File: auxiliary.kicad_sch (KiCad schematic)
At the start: 70 parts, among them IC1 MAX1708EEE+, J4 BM04B-SRSS-TB-LF-SN, J5 SM06B-SRSS-TB(LF)(SN), J6 SM09B-SRSS-TB(LF)(SN), J7 61300611121, Q1 BSS138AKA, U1 PCA9547BS,118, U2 NTS0102DP

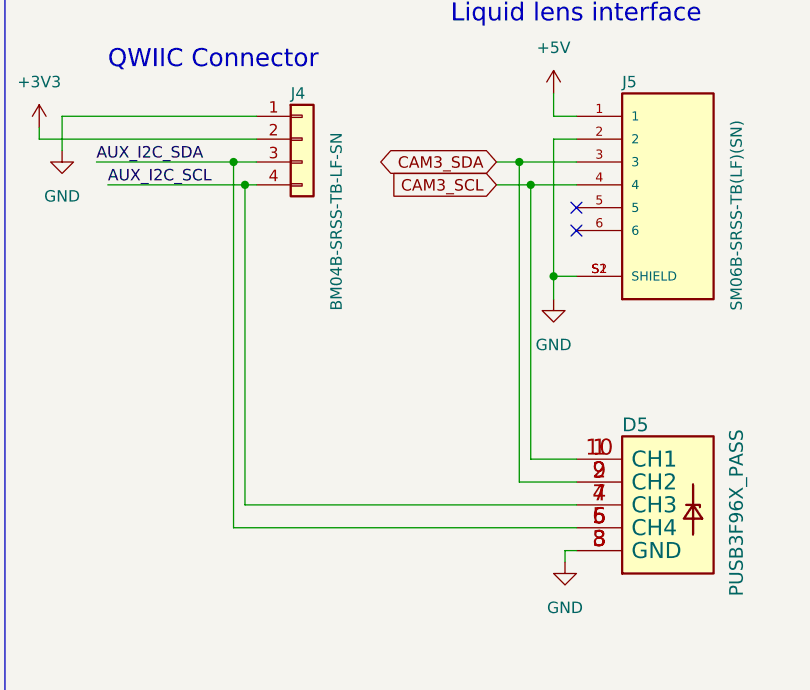
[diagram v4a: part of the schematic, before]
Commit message: Finished layout of most of the other signals, rerouted CSI
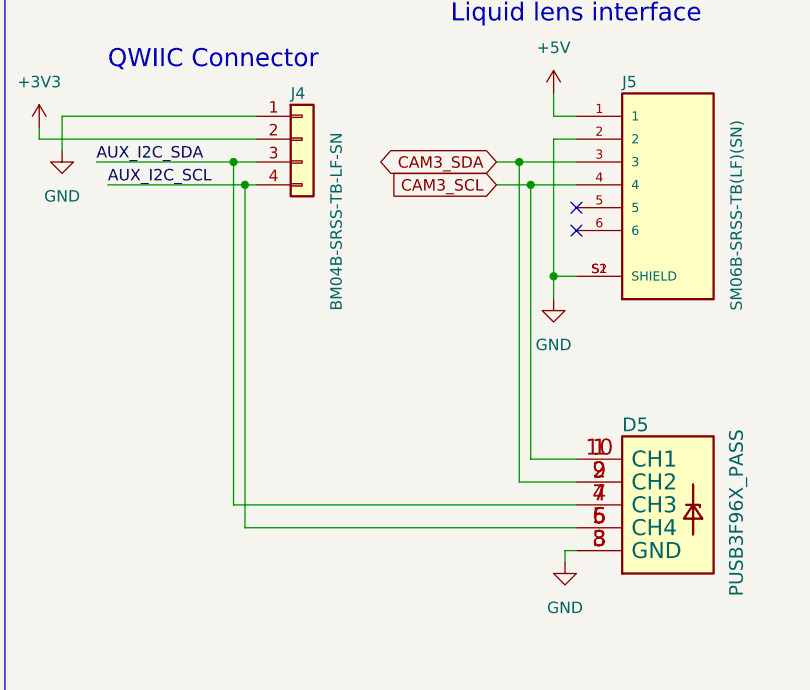
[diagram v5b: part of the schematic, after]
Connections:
- net AUX_I2C_SCL: now also D5.5 (CH4), D5.6 (CH4); no longer D5.4 (CH3), D5.7 (CH3)
- net AUX_I2C_SDA: now also D5.4 (CH3), D5.7 (CH3); no longer D5.5 (CH4), D5.6 (CH4)
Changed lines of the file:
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@@
-    (stroke (width 0) (type default) (color 0 0 0 0))
-  )
-  (wire (pts (xy 52.07 187.96) (xy 52.07 223.52))
     (stroke (width 0) (type default) (color 0 0 0 0))
   )
@@
     (stroke (width 0) (type default) (color 0 0 0 0))
   )
+  (wire (pts (xy 50.8 223.52) (xy 88.9 223.52))
+    (stroke (width 0) (type default) (color 0 0 0 0))
+  )
   (wire (pts (xy 199.39 186.69) (xy 220.98 186.69))
-    (stroke (width 0) (type default) (color 0 0 0 0))
-  )
-  (wire (pts (xy 50.8 226.06) (xy 88.9 226.06))
     (stroke (width 0) (type default) (color 0 0 0 0))
   )
@@
     (stroke (width 0) (type default) (color 0 0 0 0))
   )
+  (wire (pts (xy 52.07 226.06) (xy 88.9 226.06))
+    (stroke (width 0) (type default) (color 0 0 0 0))
+  )
   (wire (pts (xy 223.52 53.34) (xy 223.52 52.07))
     (stroke (width 0) (type default) (color 0 0 0 0))
   )
+  (wire (pts (xy 52.07 187.96) (xy 52.07 226.06))
+    (stroke (width 0) (type default) (color 0 0 0 0))
+  )
   (wire (pts (xy 372.11 134.62) (xy 374.65 134.62))
     (stroke (width 0) (type default) (color 0 0 0 0))
@@
     (stroke (width 0) (type default) (color 0 0 0 0))
   )
-  (wire (pts (xy 50.8 185.42) (xy 50.8 226.06))
+  (wire (pts (xy 50.8 185.42) (xy 50.8 223.52))
     (stroke (width 0) (type default) (color 0 0 0 0))
   )
@@
     (stroke (width 0) (type default) (color 0 0 0 0))
   )
-  (wire (pts (xy 52.07 223.52) (xy 88.9 223.52))
-    (stroke (width 0) (type default) (color 0 0 0 0))
-  )

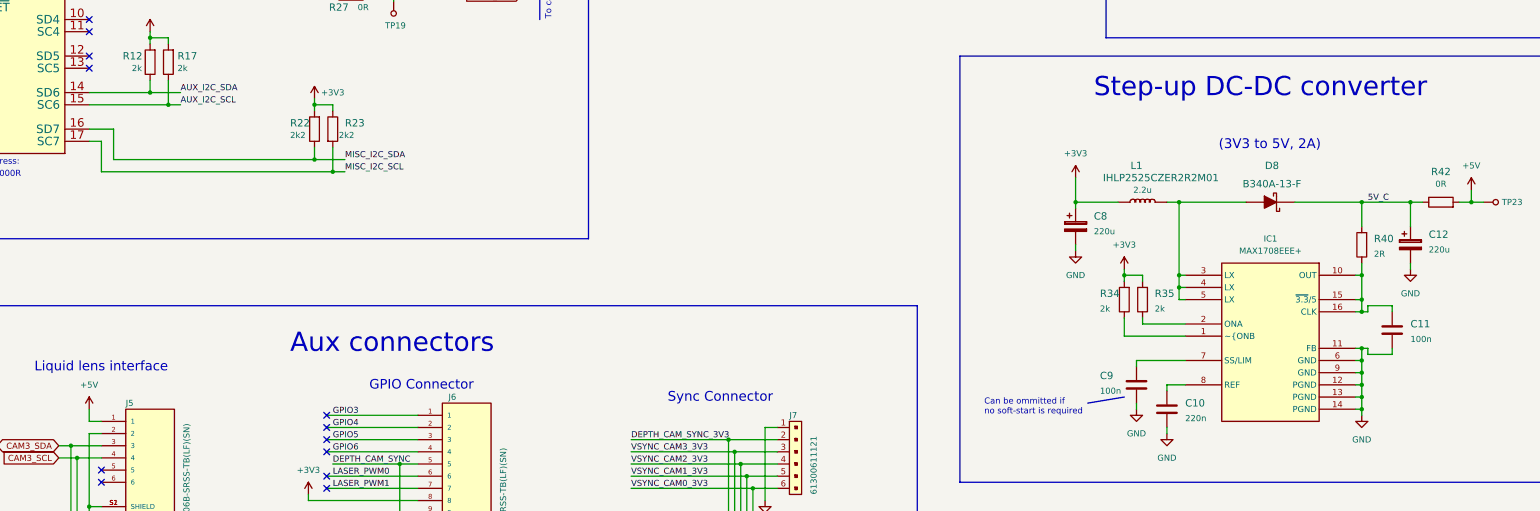
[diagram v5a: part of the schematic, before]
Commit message: Replaced some components with larger package, routed more signals
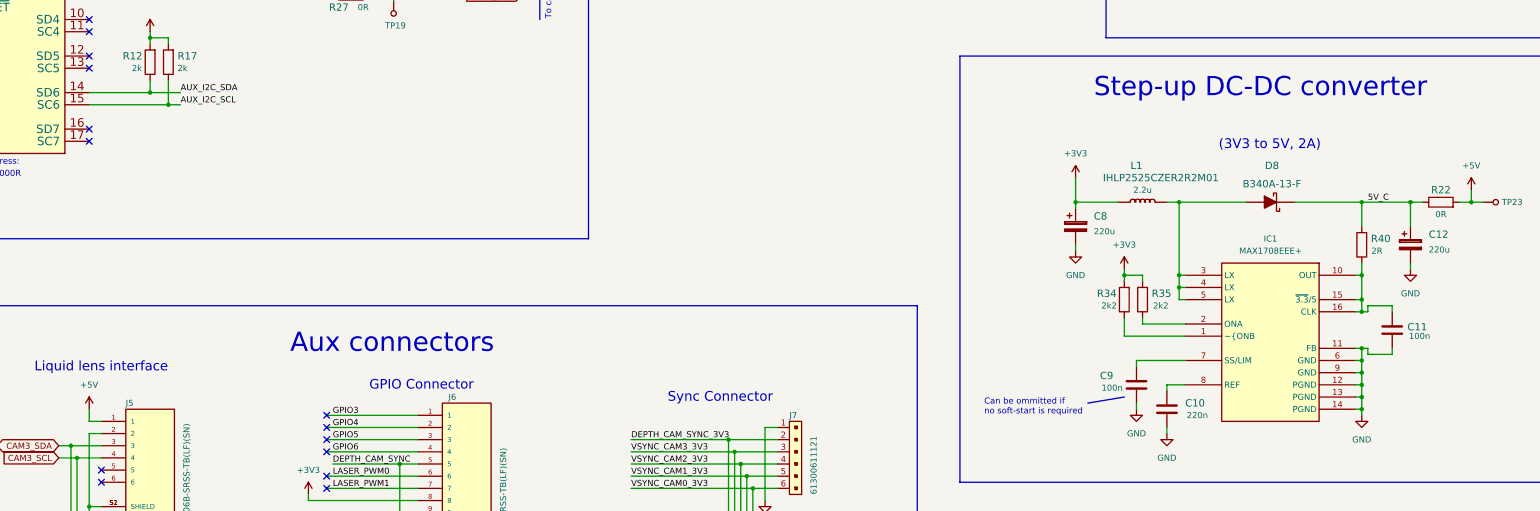
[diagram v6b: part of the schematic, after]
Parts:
- removed R22, R23: R_2k2_0402, antmicro-footprints:0402-res, symbol antmicroResistors0402:R_2k2_0402
- removed R42: R_0R_0402, antmicro-footprints:0402-res, symbol antmicroResistors0402:R_0R_0402
- added R22: R_0R_0805, antmicro-footprints:0805-res, symbol antmicroResistorsmisc:R_0R_0805
- C10: footprint antmicro-footprints:0402-cap -> antmicro-footprints:0603-cap; symbol antmicroCapacitors0402:C_220n_0402 -> antmicroCapacitors0603:C_220n_0603; MPN CC0402KRX5R6BB224 -> 0603B224K100CT; Manufacturer Yaego -> WALSIN
- C11, C9: footprint antmicro-footprints:0402-cap -> antmicro-footprints:0603-cap; symbol antmicroCapacitors0402:C_100n_0402 -> antmicroCapacitors0603:C_100n_0603; MPN GRM155R61H104KE14D -> 0603YC104KAZ2A; Manufacturer Murata -> AVX
- R34, R35: footprint antmicro-footprints:0402-res -> antmicro-footprints:0603-res; symbol antmicroResistors0402:R_2k_0402 -> antmicroResistors0603:R_2k2_0603; MPN CRCW04022K00FKED -> MCMR06X2201FTL; Manufacturer VISHAY -> MULTICOMP; Val 2k -> 2k2
- R40: footprint antmicro-footprints:0402-res -> antmicro-footprints:0603-res; symbol antmicroResistors0402:R_2R_0402 -> antmicroResistors0603:R_2R_0603; MPN CRCW04022R00FKED -> MCSR06W2R00FTL; Manufacturer Vishay -> MULTICOMP
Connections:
- net +5V: now also R22.2
- net 5V_C: now also R22.1
- net MISC_I2C_SCL: no longer names the net of U1.17 (SC7)
- net MISC_I2C_SDA: no longer names the net of U1.16 (SD7)
- no-connect marks 12 -> 14

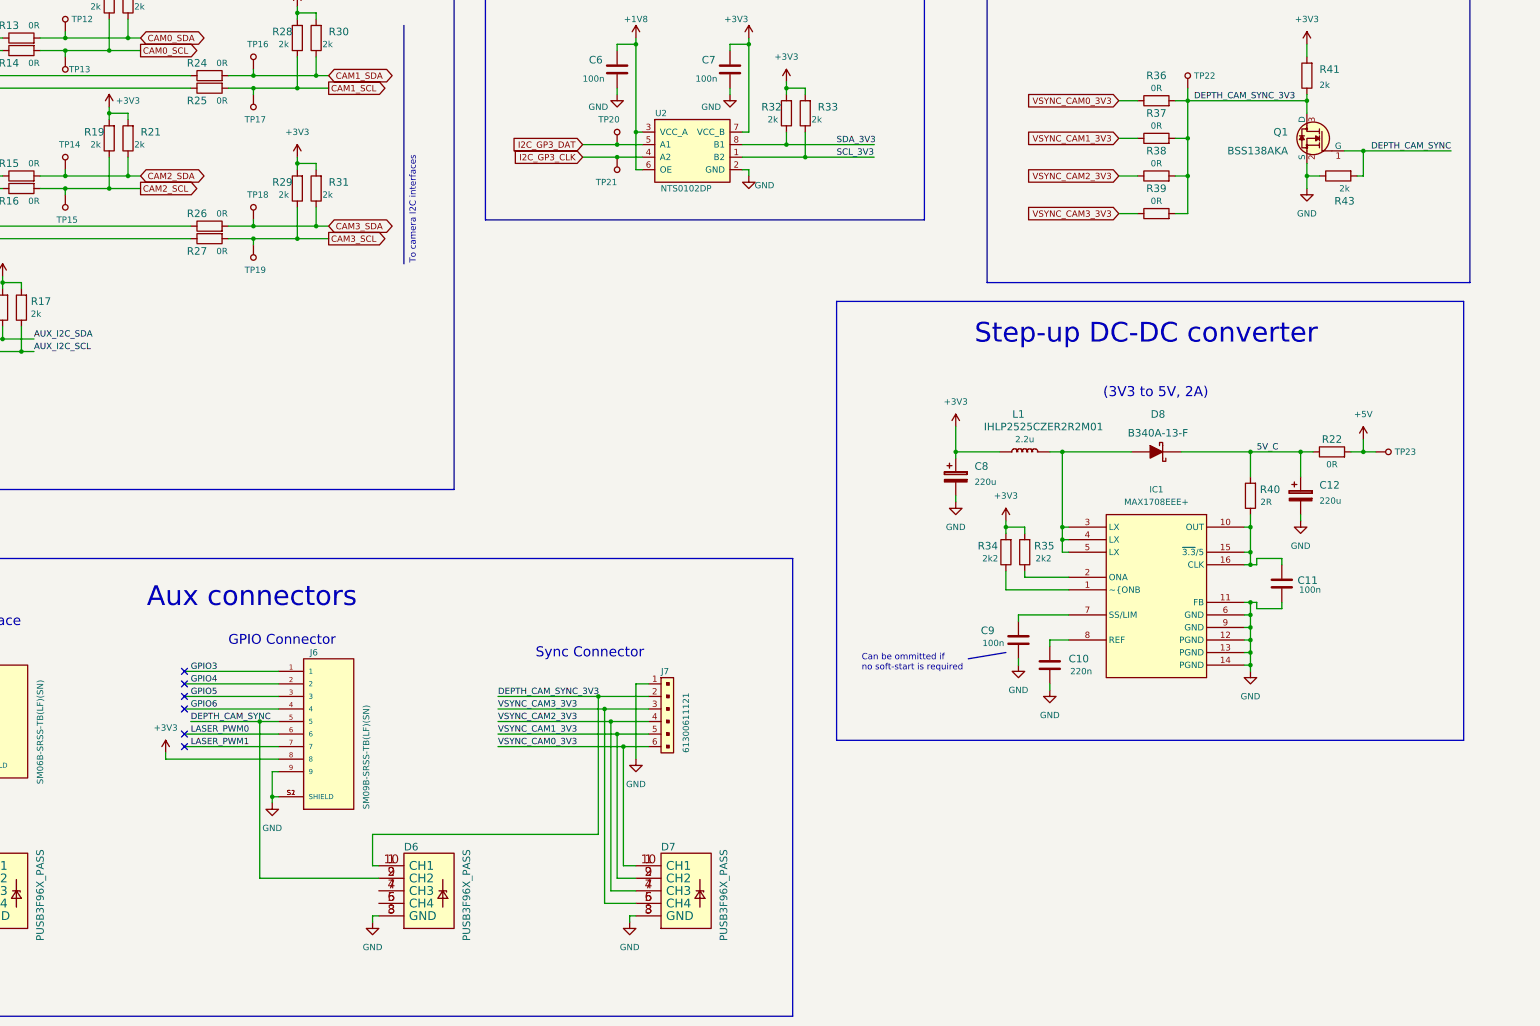
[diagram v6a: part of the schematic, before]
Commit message: Removed AUX connector and changed SYNC connector package
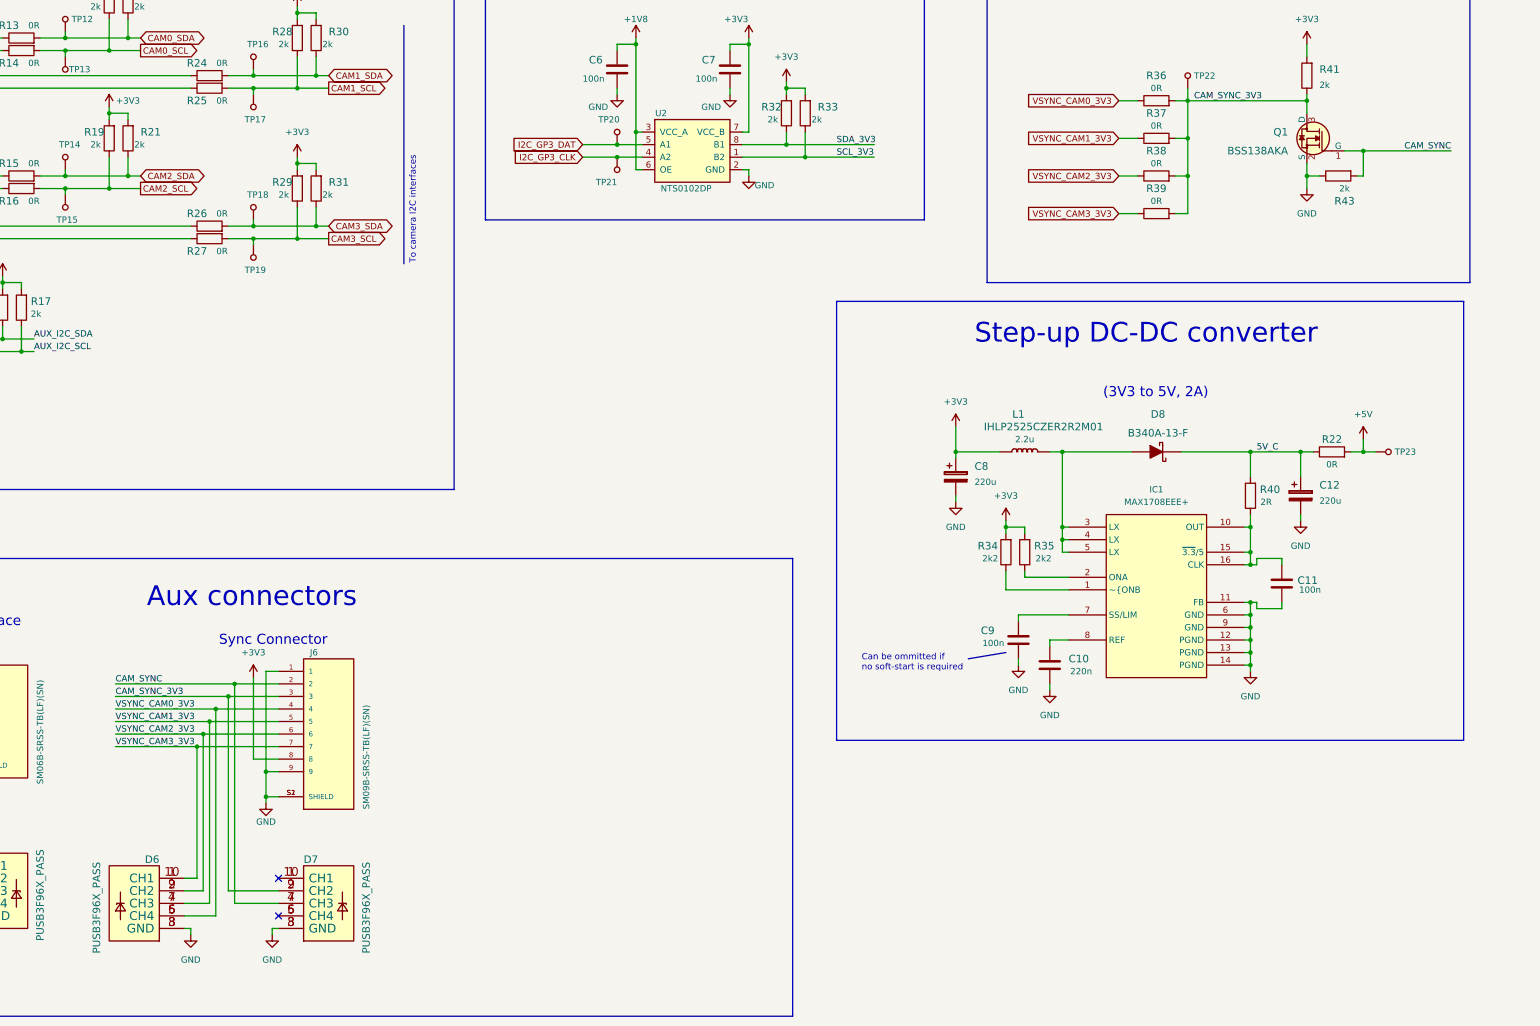
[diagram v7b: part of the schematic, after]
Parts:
- removed J7: 61300611121, antmicro-footprints:61300611121, symbol antmicroRectangularConnectorsHeadersMalePins:61300611121
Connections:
- net GPIO3 is gone; now on net GND: J6.1
- net GPIO5 is gone; now on net CAM_SYNC_3V3: J6.3
- net GPIO6 is gone; now on net VSYNC_CAM0_3V3: J6.4
- net LASER_PWM0 is gone; now on net VSYNC_CAM2_3V3: J6.6
- net LASER_PWM1 is gone; now on net VSYNC_CAM3_3V3: J6.7
- net VSYNC_CAM0_3V3: now also D6.5 (CH4), D6.6 (CH4); no longer D7.1 (CH1), D7.10 (CH1)
- net VSYNC_CAM1_3V3: now also D6.4 (CH3), D6.7 (CH3), J6.5; no longer D7.2 (CH2), D7.9 (CH2)
- net VSYNC_CAM2_3V3: now also D6.2 (CH2), D6.9 (CH2); no longer D7.4 (CH3), D7.7 (CH3)
- net VSYNC_CAM3_3V3: now also D6.1 (CH1), D6.10 (CH1); no longer D7.5 (CH4), D7.6 (CH4)
- removed net DEPTH_CAM_SYNC: D6.2 (CH2), D6.9 (CH2), J6.5, Q1.1 (G), R43.2
- net DEPTH_CAM_SYNC_3V3 renamed CAM_SYNC_3V3
- net CAM_SYNC_3V3: now also D7.2 (CH2), D7.9 (CH2); no longer D6.1 (CH1), D6.10 (CH1)
- net GPIO4 renamed CAM_SYNC
- net CAM_SYNC: now also D7.4 (CH3), D7.7 (CH3), Q1.1 (G), R43.2
- new net: D7.1 (CH1), D7.10 (CH1)
- new net: D7.5 (CH4), D7.6 (CH4)
- no-connect marks 14 -> 10
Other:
- note removed: "GPIO Connector"
- moved on the sheet: D6, D7
